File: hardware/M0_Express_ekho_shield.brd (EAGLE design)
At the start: 51.3 x 53.3 mm, 56 parts, among them SW1 KMR2, U2 AP2112-3.3, U7 LTC2058, U9 ADP1613, X3 microUSB, X4 32.768

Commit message: final schematic
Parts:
- removed C12, C3: 0.1uF, tiny_passives:0603@1
- removed R10: 1.91M, tiny_passives:0603
- removed R11: 22k, tiny_passives:0603
- removed R12: 10k, tiny_passives:0603
- removed U$3: SCREW_CONNECTOR-2PIN', BaseApp:SCREW_CONNECTOR-2PIN-3.5MM
- removed U7: LTC2058, sorber:MSOP12
- added OP1: LT1797, LT1797:TSOT23-8
- added R3: 470, SparkFun-Passives:0805
- added R6: 3M, tiny_passives:0603
- added R7: 1M, tiny_passives:0603
- R8: value 470 -> 2.2k; device SparkFun-Passives:0805 -> tiny_passives:0603
- R9: value 4.22M -> 1k
- moved R9 124.9 mm to (-16.8, -67.3)
- moved R8 114.6 mm to (-7.11, -64.0), turned to 0 degrees
- moved D4 25.8 mm to (13.0, 38.9)
- moved JP12 25.8 mm to (16.5, 36.8)
- moved L1 25.8 mm to (5.75, 40.8)
- moved R16 25.8 mm to (21.3, 45.8)
- moved R17 25.8 mm to (13.7, 43.4)
- moved C15 25.8 mm to (21.0, 40.9)
- moved C16 25.8 mm to (18.1, 38.6)
- moved C18 25.8 mm to (12.7, 32.1)
- moved C19 25.8 mm to (21.4, 43.5)
- moved JP13 25.8 mm to (18.5, 36.8)
- moved R18 25.8 mm to (13.8, 45.3)
- moved U9 25.8 mm to (17.5, 43.0)
- moved C21 8.64 mm to (35.1, 28.1)
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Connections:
- removed net AMPOUT: R11.1, R8.1, U7.3
- removed net INA-: R11.2, R12.2, U7.5
- removed net VS_AMP: JP1.2, U7.10, U7.8
- new net HARVESTER_IN: OP1.1, R3.1, R8.2
- new net N$5: OP1.4, R8.1, R9.2
- net AVCC_SET: now also OP1.5; no longer C3.1, U7.11
- net GND: now also OP1.2, R7.2, R9.1; no longer C12.2, C3.2, R10.2, R12.1, U$3.P$1, U7.2, U7.EXP
- net LOAD_V+: now also JP1.2, R3.2, R6.1; no longer R8.2, R9.1, U$3.P$2
- net VDAC: now also OP1.3; no longer C12.1, U7.6
- net VS_ADC: now also R6.2, R7.1; no longer R10.1, R9.2, U7.7
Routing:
- net VDAC: track 21.7 -> 0.00 mm, vias 1 -> 0
- net AMPOUT: track 16.4 -> 0.00 mm, vias 2 -> 0
- net VS_ADC: track 16.1 -> 0.00 mm
- net VS_AMP: track 13.5 -> 0.00 mm, vias 1 -> 0
- net LOAD_V+: track 12.8 -> 0.00 mm
- net INA-: track 6.07 -> 0.00 mm
- net AVCC_SET: track 7.62 -> 2.00 mm
- net GND: track 10.9 -> 9.93 mm, vias 29 -> 20
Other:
- board text removed: "CLK"
- board text removed: "CP/2"
- board text removed: "CS"
- board text removed: "PF"
- board text removed: "RD"
- board text removed: "SIMO"
- board text removed: "SOMI"
- board text removed: "WR"

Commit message: final ekho hardware done
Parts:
- removed SW1: KMR2, microbuilder:BTN_KMR2_4.6X2.8
- removed X3: microUSB, microbuilder:4UCONN_20329_V2
- added C2: 1uF, microbuilder:0603-NO
- added J1: MF-CON-MICROUSB-RIGHT, MF_Connectors:MICROUSB-RIGHT
- added S3: TL1015AF, eswitch:TS1015
- JP12, JP13: device SparkFun-Connectors:1X02-1.27MM -> SparkFun-Connectors:1X02_LOCK
- moved R9 114.9 mm to (23.9, 40.1), turned to 270 degrees
- moved R3 110.5 mm to (29.7, 35.8)
- moved R8 109.3 mm to (29.2, 39.1), turned to 270 degrees
- moved R6 109.1 mm to (32.5, 34.8), turned to 270 degrees
- moved R7 105.7 mm to (29.7, 33.8), turned to 180 degrees
- moved OP1 98.7 mm to (25.4, 36.8), turned to 90 degrees
- moved R2 47.4 mm to (37.3, 24.1), turned to 90 degrees
- moved R5 47.3 mm to (35.8, 25.7), turned to 90 degrees
- moved LED1 47.2 mm to (37.3, 26.9)
- moved LED2 47.0 mm to (35.8, 28.7)
- moved U$1 40.6 mm to (49.3, 12.7)
- moved JP2 38.3 mm to (20.0, 9.32), turned to 270 degrees
- moved C21 3.21 mm to (31.9, 27.7), turned to 90 degrees
- moved JP13 1.63 mm to (19.7, 35.8)
- moved R1 1.55 mm to (8.64, 24.9)
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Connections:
- removed net N$1: R5.1, U$14.6
- removed net N$2: R2.1, U$14.5
- new net LED1: R2.1, U$14.29
- new net LED2: R5.1, U$14.30
- net !RESET: now also S3.2; no longer SW1.A, SW1.A'
- net AVCC_SET: now also C2.1
- net D+: now also J1.3; no longer X3.D+
- net D-: now also J1.2; no longer X3.D-
- net GND: now also C2.2, J1.5, J1.S1, J1.S2, J1.S3, J1.S4, J1.S5, J1.S6, S3.1, S3.G1, S3.G2, S3.G3, S3.G4; no longer SW1.B, SW1.B', X3.BASE@1, X3.BASE@2, X3.GND, X3.SPRT@1, X3.SPRT@2, X3.SPRT@3, X3.SPRT@4
- net TDI/RX_DEBUG: now also U$14.14; no longer U$14.64
- net TDO/TX_DEBUG: now also U$14.13; no longer U$14.63
- net VBUS: now also J1.1; no longer X3.VBUS
- net VS_ADC: now also U$14.20; no longer U$14.13
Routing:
- net +3V3: track 80.1 -> 24.9 mm, vias 4 -> 9
- net VBUS: track 27.8 -> 80.6 mm, vias 3 -> 4
- net VDAC: track 0.00 -> 29.7 mm, vias 0 -> 2
- net VS_ADC: track 0.00 -> 25.9 mm
- net TDI/RX_DEBUG: track 0.00 -> 24.0 mm
- net TDO/TX_DEBUG: track 0.00 -> 21.4 mm
- net LOAD_V+: track 0.00 -> 20.1 mm
- net SWDCLK: track 9.11 -> 21.3 mm
- net !RESET: track 29.9 -> 39.5 mm
- net AVCC_SET: track 2.00 -> 10.3 mm
- net EN: track 10.6 -> 2.83 mm
- net N$5: track 0.00 -> 7.17 mm
- net SWDIO: track 7.51 -> 14.5 mm
- net HARVESTER_IN: track 0.00 -> 4.65 mm
- net LED1: track 0.00 -> 2.97 mm
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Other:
- board text added: "Ekho Shield Rev A. for CircuitPython TU Delft Northwestern U Design: Josiah Hester"
- board text added: "Extended Ekho Shield"
- board text added: "RST"
- board text removed: "+"
- board text removed: "+12V"
- board text removed: "-"
- board text removed: "EH Shield Rev A. for CircuitPython Design: Josiah Hester"
- board text removed: "Extended"
- board text removed: "LOAD"

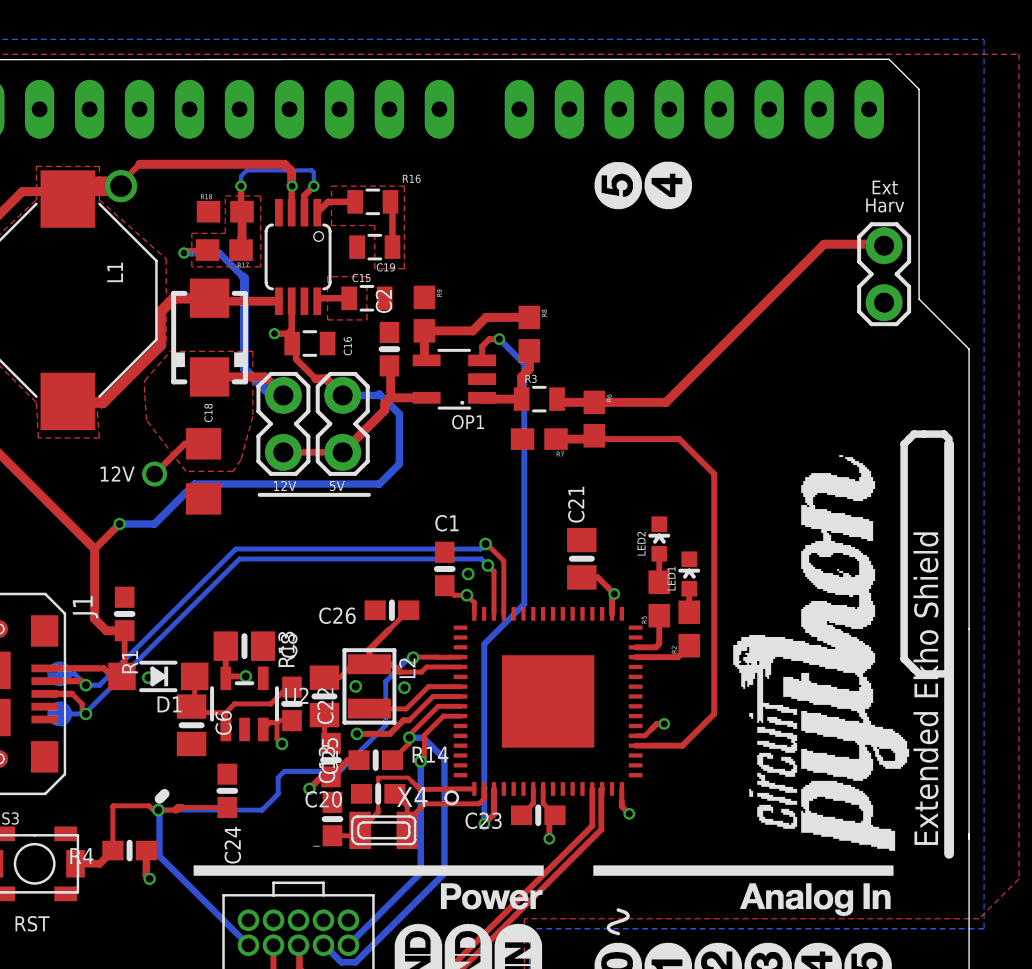
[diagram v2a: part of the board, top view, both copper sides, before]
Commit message: can measure current and communicate/takeover the M0 kind of like a debugger
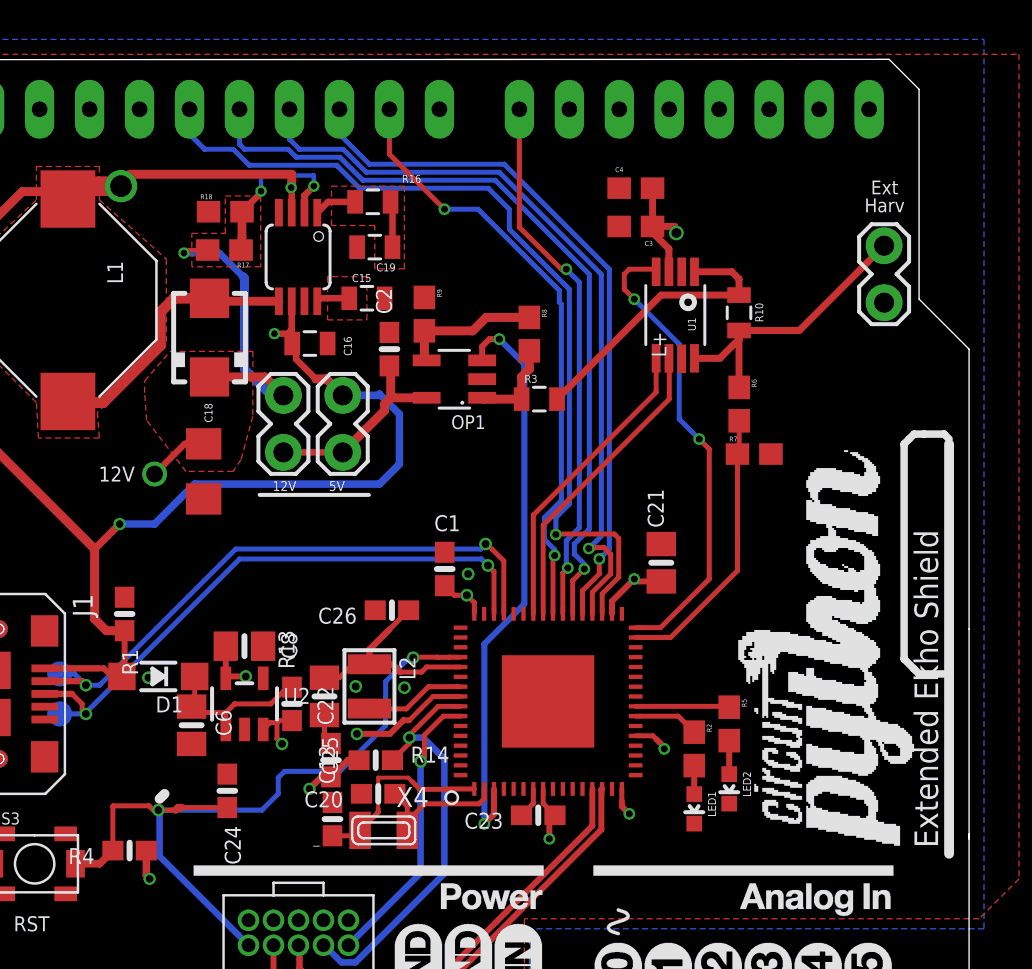
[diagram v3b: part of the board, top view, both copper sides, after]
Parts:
- added C3: 0.1uF, tiny_passives:0603
- added C4: 1.0uF, tiny_passives:0603
- added R10: 10, SparkFun-Passives:0805
- added U1: INA225, ina225:MSOP8
- R3: value 470 -> 100
- moved LED2 13.2 mm to (39.4, 16.0), turned to 180 degrees
- moved LED1 11.9 mm to (37.6, 15.0), turned to 180 degrees
- moved R7 10.9 mm to (40.6, 33.0), turned to 0 degrees
- moved R6 7.41 mm to (39.9, 35.6)
- moved R5 7.28 mm to (39.4, 19.3), turned to 270 degrees
- moved R2 6.10 mm to (37.6, 18.0), turned to 270 degrees
- moved C21 4.04 mm to (35.9, 27.5)
- moved U$1 0.36 mm to (49.5, 13.0)
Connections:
- removed net A0: JP_AD.1
- removed net A1: JP_AD.2
- removed net A2: JP_AD.3
- removed net A3: JP_AD.4
- removed net LOAD_V+: JP1.2, R3.2, R6.1
- new net CSG0: U$14.42, U1.5
- new net CSG1: U$14.41, U1.6
- new net CS_ADC: U$14.32, U1.4
- new net HIGH_LOAD_V+: R10.1, R3.2, U1.1
- new net LOW_LOAD_V+: JP1.2, R10.2, R6.1, U1.8
- net +3V3: now also C3.1, C4.1, U1.3
- net GND: now also C3.2, C4.2, U1.2, U1.7
- net LED1: now also U$14.23; no longer U$14.29
- net LED2: now also U$14.24; no longer U$14.30
- net NV_CLK: now also U$14.35
- net NV_CS: now also U$14.37
- net NV_READ: now also U$14.39
- net NV_SIMO: now also U$14.36
- net NV_SOMI: now also U$14.38
- net NV_WRITE: now also U$14.40
- net VS_ADC: now also U$14.31; no longer U$14.20
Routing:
- net NV_CLK: track 0.00 -> 44.7 mm, vias 0 -> 1
- net NV_SOMI: track 0.00 -> 40.3 mm, vias 0 -> 1
- net NV_SIMO: track 0.00 -> 39.1 mm, vias 0 -> 1
- net NV_CS: track 0.00 -> 35.9 mm, vias 0 -> 1
- net NV_WRITE: track 0.00 -> 30.9 mm, vias 0 -> 2
- net NV_READ: track 0.00 -> 27.5 mm, vias 0 -> 2
- net CS_ADC: track 0.00 -> 23.8 mm, vias 0 -> 2
- net LOAD_V+: track 20.1 -> 0.00 mm
- net CSG1: track 0.00 -> 15.7 mm
- net CSG0: track 0.00 -> 15.6 mm
- net LOW_LOAD_V+: track 0.00 -> 14.7 mm
- net HIGH_LOAD_V+: track 0.00 -> 14.7 mm
- net VS_ADC: track 25.9 -> 14.2 mm
- net +3V3: track 24.9 -> 31.9 mm, vias 9 -> 10
- net LED2: track 2.71 -> 4.78 mm
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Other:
- board text added: "L+"
